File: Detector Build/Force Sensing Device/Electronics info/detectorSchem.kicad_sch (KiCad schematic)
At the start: 28 parts

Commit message: added more info and started work on some info
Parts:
- R?: value 10k(maybe changed to 100k) -> 100K
- R?: value 10k(maybe changed to 100k) -> 10k
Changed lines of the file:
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@@
   (symbol (lib_id "Device:R_Small_US") (at 73.66 26.67 0) (unit 1)
     (in_bom yes) (on_board yes) (fields_autoplaced)
-    (property "Reference" "R?" (id 0) (at 75.311 25.7615 0)
-      (effects (font (size 1.27 1.27)) (justify left))
-    )
-    (property "Value" "10k(maybe changed to 100k)" (id 1) (at 75.311 28.5366 0)
+    (property "Reference" "R?" (id 0) (at 76.2 25.3999 0)
+      (effects (font (size 1.27 1.27)) (justify left))
+    )
+    (property "Value" "100K" (id 1) (at 76.2 27.9399 0)
       (effects (font (size 1.27 1.27)) (justify left))
     )
@@
   (symbol (lib_id "Device:R_Small_US") (at 73.66 102.87 0) (unit 1)
     (in_bom yes) (on_board yes) (fields_autoplaced)
-    (property "Reference" "R?" (id 0) (at 75.311 101.9615 0)
-      (effects (font (size 1.27 1.27)) (justify left))
-    )
-    (property "Value" "10k(maybe changed to 100k)" (id 1) (at 75.311 104.7366 0)
+    (property "Reference" "R?" (id 0) (at 76.2 101.5999 0)
+      (effects (font (size 1.27 1.27)) (justify left))
+    )
+    (property "Value" "10k" (id 1) (at 76.2 104.1399 0)
       (effects (font (size 1.27 1.27)) (justify left))
     )
@@
     )
     (path "/2e8dbda0-cfae-4f3f-8632-81c2c998844f"
-      (reference "R?") (unit 1) (value "10k(maybe changed to 100k)") (footprint "")
+      (reference "R?") (unit 1) (value "100K") (footprint "")
     )
     (path "/4629111a-2178-479e-bfdd-468e3179d49e"
@@
     )
     (path "/78620eb8-ad4c-482d-b1a5-6c31619b2879"
-      (reference "R?") (unit 1) (value "10k(maybe changed to 100k)") (footprint "")
+      (reference "R?") (unit 1) (value "10k") (footprint "")
     )
     (path "/84d4acf2-95da-4bde-aaf9-948b78559314"

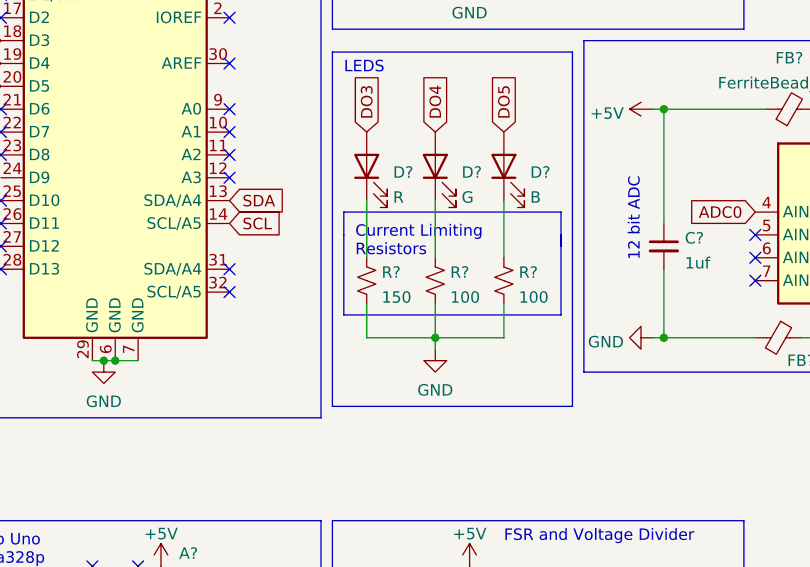
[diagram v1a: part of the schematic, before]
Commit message: updated the resistor values
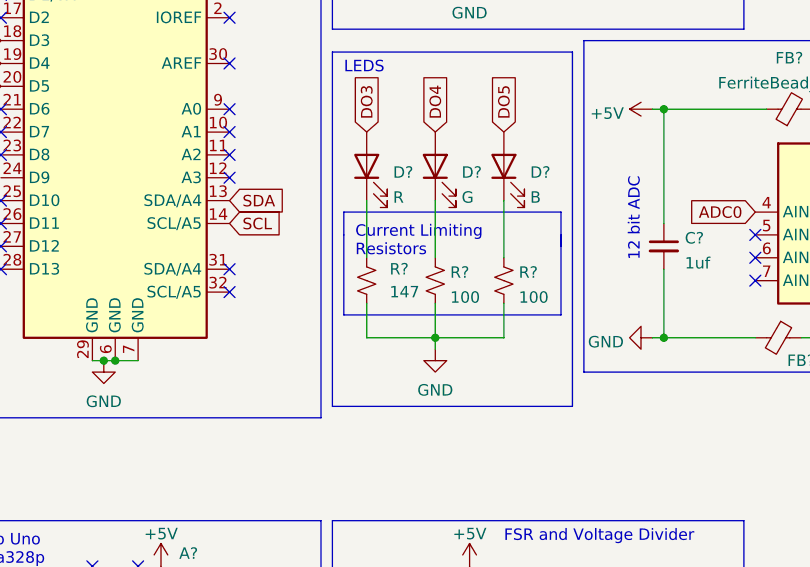
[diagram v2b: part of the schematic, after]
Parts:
- R?: value 150 -> 147
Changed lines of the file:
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@@
   (symbol (lib_id "Device:R_Small_US") (at 62.23 63.5 0) (unit 1)
     (in_bom yes) (on_board yes) (fields_autoplaced)
-    (property "Reference" "R?" (id 0) (at 63.881 62.5915 0)
-      (effects (font (size 1.27 1.27)) (justify left))
-    )
-    (property "Value" "150" (id 1) (at 63.881 65.3666 0)
+    (property "Reference" "R?" (id 0) (at 64.77 62.2299 0)
+      (effects (font (size 1.27 1.27)) (justify left))
+    )
+    (property "Value" "147" (id 1) (at 64.77 64.7699 0)
       (effects (font (size 1.27 1.27)) (justify left))
     )
@@
     )
     (path "/5bb9bcec-9f60-4a36-b646-41b2d53c7226"
-      (reference "R?") (unit 1) (value "150") (footprint "")
+      (reference "R?") (unit 1) (value "147") (footprint "")
     )
     (path "/60b868e3-a9f8-4d20-ae5a-40ca53af4adb"

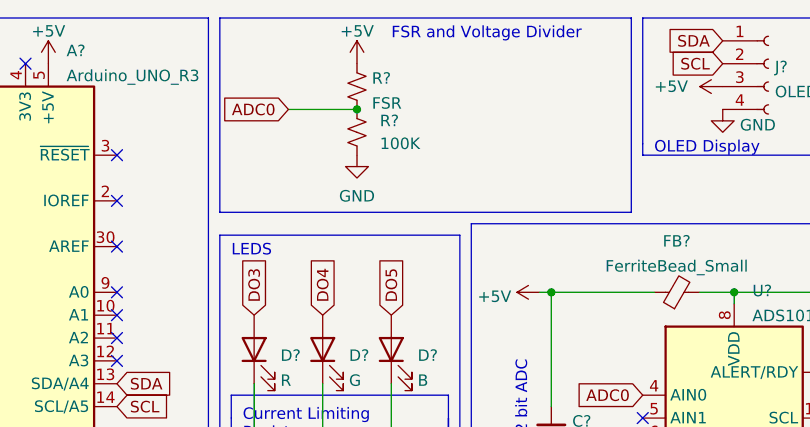
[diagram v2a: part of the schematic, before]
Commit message: added more info to readme and reverted change to voltage divider
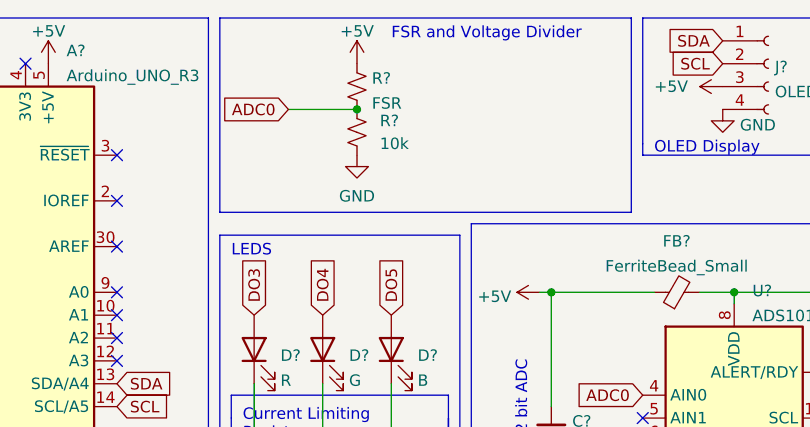
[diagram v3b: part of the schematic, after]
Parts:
- R?: value 100K -> 10k
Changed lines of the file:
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@@
       (effects (font (size 1.27 1.27)) (justify left))
     )
-    (property "Value" "100K" (id 1) (at 76.2 27.9399 0)
+    (property "Value" "10k" (id 1) (at 76.2 27.9399 0)
       (effects (font (size 1.27 1.27)) (justify left))
     )
@@
     )
     (path "/2e8dbda0-cfae-4f3f-8632-81c2c998844f"
-      (reference "R?") (unit 1) (value "100K") (footprint "")
+      (reference "R?") (unit 1) (value "10k") (footprint "")
     )
     (path "/4629111a-2178-479e-bfdd-468e3179d49e"
